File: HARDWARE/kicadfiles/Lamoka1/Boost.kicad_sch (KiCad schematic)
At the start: 50 parts, among them J1 Boostconverteroutput, J2 Boostconverterinput, J3 Groundconnection, Q1 CSD19531Q5A, Q2 CSD19531Q5A, Q3 CSD19531Q5A, Q4 CSD19531Q5A, Q5 AO3400A, U2 LM5122QMHE/NOPB, U3 LM5122QMHE/NOPB

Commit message: Reconfiguring the BOM, other misc tasks
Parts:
- C27: footprint Components:PCAP_10x10-ELECT_NCA -> Components:PCAP_8x10-ELECT_NCH
- C36: footprint Components:CAP_UCD2A_NCH -> Components:PCAP_8x10-ELECT_NCH
- J1, J2, J3, TP1, TP2, TP3, TP4, TP5, TP6, TP7, TP8: now left out of the parts list
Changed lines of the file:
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@@
 		(body_style 1)
 		(exclude_from_sim no)
-		(in_bom yes)
+		(in_bom no)
 		(on_board yes)
 		(in_pos_files yes)
@@
 		(body_style 1)
 		(exclude_from_sim no)
-		(in_bom yes)
+		(in_bom no)
 		(on_board yes)
 		(in_pos_files yes)
@@
 			)
 		)
-		(property "Datasheet" "C1206C224M1REC7210"
+		(property "Datasheet" "MPN: C1206C224M1REC7210"
 			(at 110.49 138.43 0)
 			(hide yes)
@@
 			)
 		)
-		(property "Datasheet" "https://search.murata.co.jp/Ceramy/image/img/A01X/G101/ENG/KRM55_25V-100V_E.pdf"
+		(property "Datasheet" "MPN: KRM55WR72A226MH01K"
 			(at 452.73 147.32 0)
 			(hide yes)
@@
 			)
 		)
-		(property "Datasheet" "RC0603FR-0736KL"
+		(property "Datasheet" "MPN: RC0603FR-0736KL"
 			(at 151.13 176.53 0)
 			(hide yes)
@@
 		(body_style 1)
 		(exclude_from_sim no)
-		(in_bom yes)
+		(in_bom no)
 		(on_board yes)
 		(in_pos_files yes)
@@
 			)
 		)
-		(property "Datasheet" "https://www.diodes.com/assets/Datasheets/SDM1U100S1F.pdf"
+		(property "Datasheet" "MPN: SDM1U100S1F-7"
 			(at -150.47 154.94 0)
 			(hide yes)
@@
 		(body_style 1)
 		(exclude_from_sim no)
-		(in_bom yes)
+		(in_bom no)
 		(on_board yes)
 		(in_pos_files yes)
@@
 			)
 		)
-		(property "Datasheet" "RN73R1JTTD4992F25"
+		(property "Datasheet" "MPN: RN73R1JTTD4992F25"
 			(at 35.56 30.48 0)
 			(hide yes)
@@
 			)
 		)
-		(property "Datasheet" "http://www.ti.com/lit/gpn/csd19531q5a"
+		(property "Datasheet" "MPN: CSD19531Q5A"
 			(at 113.03 40.64 0)
 			(hide yes)
@@
 			)
 		)
-		(property "Datasheet" "https://www.diodes.com/assets/Datasheets/SDM1U100S1F.pdf"
+		(property "Datasheet" "MPN: SDM1U100S1F-7"
 			(at -92.05 154.94 0)
 			(hide yes)
@@
 			)
 		)
-		(property "Datasheet" "RC0603FR-0756K2L"
+		(property "Datasheet" "MPN: RC0603FR-0756K2L"
 			(at 243.84 116.84 0)
 			(hide yes)
@@
 		(body_style 1)
 		(exclude_from_sim no)
-		(in_bom yes)
+		(in_bom no)
 		(on_board yes)
 		(in_pos_files yes)
@@
 			)
 		)
-		(property "Datasheet" "UUX2A470MNL1GS"
+		(property "Datasheet" "MPN: UUX2A470MNL1GS"
 			(at 27.94 64.77 0)
 			(hide yes)
@@
 			)
 		)
-		(property "Footprint" "Components:PCAP_10x10-ELECT_NCA"
+		(property "Footprint" "Components:PCAP_8x10-ELECT_NCH"
 			(at 36.83 63.5 0)
 			(hide yes)
@@
 			)
 		)
-		(property "Datasheet" "UCD2A220MNL1GS"
+		(property "Datasheet" "MPN: UCD2A220MNL1GS"
 			(at 36.83 63.5 0)
 			(hide yes)
@@
 		(body_style 1)
 		(exclude_from_sim no)
-		(in_bom yes)
+		(in_bom no)
 		(on_board yes)
 		(in_pos_files yes)
@@
 		(body_style 1)
 		(exclude_from_sim no)
-		(in_bom yes)
+		(in_bom no)
 		(on_board yes)
 		(in_pos_files yes)
@@
 			)
 		)
-		(property "Datasheet" "https://product.tdk.com/system/files/dam/doc/product/capacitor/ceramic/mlcc/catalog/mlcc_commercial_soft_cnc_en.pdf"
+		(property "Datasheet" "MPN: CNC5L1X7R1H106K160AE"
 			(at 91.44 334.62 0)
 			(hide yes)
@@
 		(body_style 1)
 		(exclude_from_sim no)
-		(in_bom yes)
+		(in_bom no)
 		(on_board yes)
 		(in_pos_files yes)
@@
 			)
 		)
-		(property "Datasheet" "http://www.ti.com/lit/gpn/csd19531q5a"
+		(property "Datasheet" "MPN: CSD19531Q5A"
 			(at 114.3 78.74 0)
 			(hide yes)
@@
 			)
 		)
-		(property "Datasheet" "http://www.ti.com/lit/gpn/csd19531q5a"
+		(property "Datasheet" "MPN: CSD19531Q5A"
 			(at 115.57 72.39 0)
 			(hide yes)
@@
 			)
 		)
-		(property "Datasheet" "RC0603FR-0710KL"
+		(property "Datasheet" "MPN: RC0603FR-0710KL"
 			(at 182.88 154.94 0)
 			(hide yes)
@@
 			)
 		)
-		(property "Datasheet" "https://www.te.com/commerce/DocumentDelivery/DDEController?Action=srchrtrv&DocNm=1773449-4&DocType=Data+Sheet&DocLang=English&PartCntxt=1-2176422-9&DocFormat=pdf"
+		(property "Datasheet" "MPN: TLRP3A30CR005FTE"
 			(at 59.69 63.5 0)
 			(hide yes)
@@
 			)
 		)
-		(property "Datasheet" "CL10B104KB8NNNC"
+		(property "Datasheet" "MPN: CL10B104KB8NNNC"
 			(at 83.82 35.56 0)
 			(hide yes)
@@
 			)
 		)
-		(property "Footprint" "Components:CAP_UCD2A_NCH"
+		(property "Footprint" "Components:PCAP_8x10-ELECT_NCH"
 			(at 266.7 148.59 0)
 			(hide yes)
@@
 			)
 		)
-		(property "Datasheet" "UCD2A101MNJ1MS"
+		(property "Datasheet" "MPN: UUX2A100MNL1GS"
 			(at 266.7 148.59 0)
 			(hide yes)
@@
 			)
 		)
-		(property "Datasheet" "UCD2A220MNL1GS"
+		(property "Datasheet" "MPN: UCD2A220MNL1GS"
 			(at 245.11 148.59 0)
 			(hide yes)
@@
 			)
 		)
-		(property "Datasheet" "https://content.kemet.com/datasheets/KEM_C1002_X7R_SMD.pdf"
+		(property "Datasheet" "MPN: C1206C474K1RACTU"
 			(at 196.85 135.89 0)
 			(hide yes)
@@
 			)
 		)
-		(property "Datasheet" "C1206C224M1REC7210"
+		(property "Datasheet" "MPN: C1206C224M1REC7210"
 			(at 50.8 138.43 0)
 			(hide yes)
@@
 			)
 		)
-		(property "Datasheet" "https://product.tdk.com/system/files/dam/doc/product/capacitor/ceramic/mlcc/catalog/mlcc_commercial_soft_cnc_en.pdf"
+		(property "Datasheet" "MPN: CNC5L1X7R1H106K160AE"
 			(at 33.02 334.62 0)
 			(hide yes)
@@
 			)
 		)
-		(property "Datasheet" "https://www.te.com/commerce/DocumentDelivery/DDEController?Action=srchrtrv&DocNm=1773449-4&DocType=Data+Sheet&DocLang=English&PartCntxt=1-2176422-9&DocFormat=pdf"
+		(property "Datasheet" "MPN: TLRP3A30CR005FTE"
 			(at 50.8 92.71 0)
 			(hide yes)
@@
 			)
 		)
-		(property "Datasheet" "https://www.we-online.com/catalog/datasheet/7443641000B.pdf?ki"
+		(property "Datasheet" "MPN: 7443641000B"
 			(at 135.89 45.72 0)
 			(hide yes)
@@
 			)
 		)
-		(property "Datasheet" ""
+		(property "Datasheet" "MPN: RN73R1JTTD1842B25"
 			(at 48.26 30.48 0)
 			(hide yes)
@@
 			)
 		)
-		(property "Datasheet" "https://www.we-online.com/catalog/datasheet/7443641000B.pdf?ki"
+		(property "Datasheet" "MPN: 7443641000B"
 			(at 132.08 74.93 0)
 			(hide yes)
@@
 			)
 		)
-		(property "Datasheet" "https://www.ti.com/lit/gpn/lm5122-q1"
+		(property "Datasheet" "MPN: LM5122QMHE/NOPB"
 			(at 181.61 20.32 0)
 			(hide yes)
@@
 		(body_style 1)
 		(exclude_from_sim no)
-		(in_bom yes)
+		(in_bom no)
 		(on_board yes)
 		(in_pos_files yes)
@@
 			)
 		)
-		(property "Datasheet" "http://www.ti.com/lit/gpn/csd19531q5a"
+		(property "Datasheet" "MPN: CSD19531Q5A"
 			(at 114.3 34.29 0)
 			(hide yes)
@@
 		(body_style 1)
 		(exclude_from_sim no)
-		(in_bom yes)
+		(in_bom no)
 		(on_board yes)
 		(in_pos_files yes)
@@
 			)
 		)
-		(property "Datasheet" "RC0603FR-0736KL"
+		(property "Datasheet" "MPN: RC0603FR-0736KL"
 			(at 162.56 124.46 0)
 			(hide yes)
@@
 			)
 		)
-		(property "Datasheet" "RC0603FR-07392KL"
+		(property "Datasheet" "MPN: RC0603FR-07392KL"
 			(at 208.28 154.94 0)
 			(hide yes)
@@
 			)
 		)
-		(property "Datasheet" "UUX2A470MNL1GS"
+		(property "Datasheet" "MPN: UUX2A470MNL1GS"
 			(at 19.05 63.5 0)
 			(hide yes)
@@
 			)
 		)
-		(property "Datasheet" "CC0603KRX7R9BB223"
+		(property "Datasheet" "MPN: CC0603KRX7R9BB223"
 			(at 257.81 116.84 0)
 			(hide yes)
@@
 			)
 		)
-		(property "Datasheet" "https://www.ti.com/lit/gpn/lm5122-q1"
+		(property "Datasheet" "MPN: LM5122QMHE/NOPB"
 			(at 181.61 55.88 0)
 			(hide yes)
@@
 			)
 		)
-		(property "Datasheet" "RC0805FR-0747KL"
+		(property "Datasheet" "MPN: RC0805FR-0747KL"
 			(at 74.93 180.34 0)
 			(hide yes)
@@
 			)
 		)
-		(property "Datasheet" "AO3400A"
+		(property "Datasheet" "MPN: AO3400A"
 			(at 29.21 175.26 0)
 			(hide yes)
@@
 			)
 		)
-		(property "Datasheet" "RC0603FR-0736KL"
+		(property "Datasheet" "MPN: RC0603FR-0736KL"
 			(at 132.08 163.83 0)
 			(hide yes)
@@
 		(body_style 1)
 		(exclude_from_sim no)
-		(in_bom yes)
+		(in_bom no)
 		(on_board yes)
 		(in_pos_files yes)

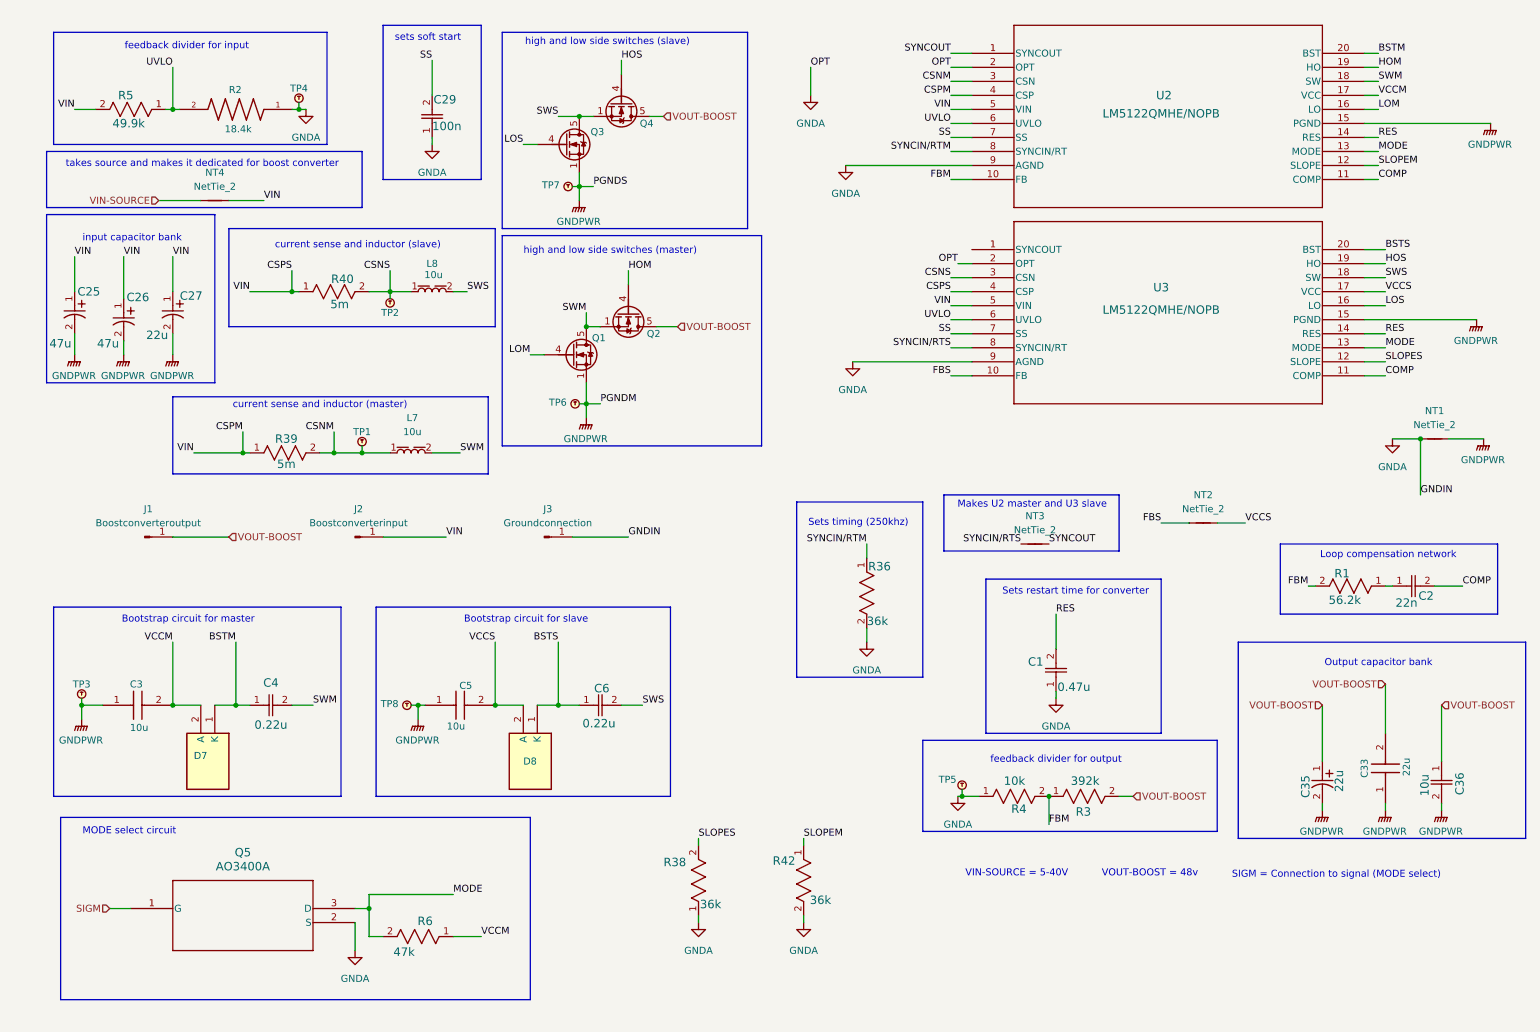
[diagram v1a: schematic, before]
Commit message: Take things out so boost converter can be standalone
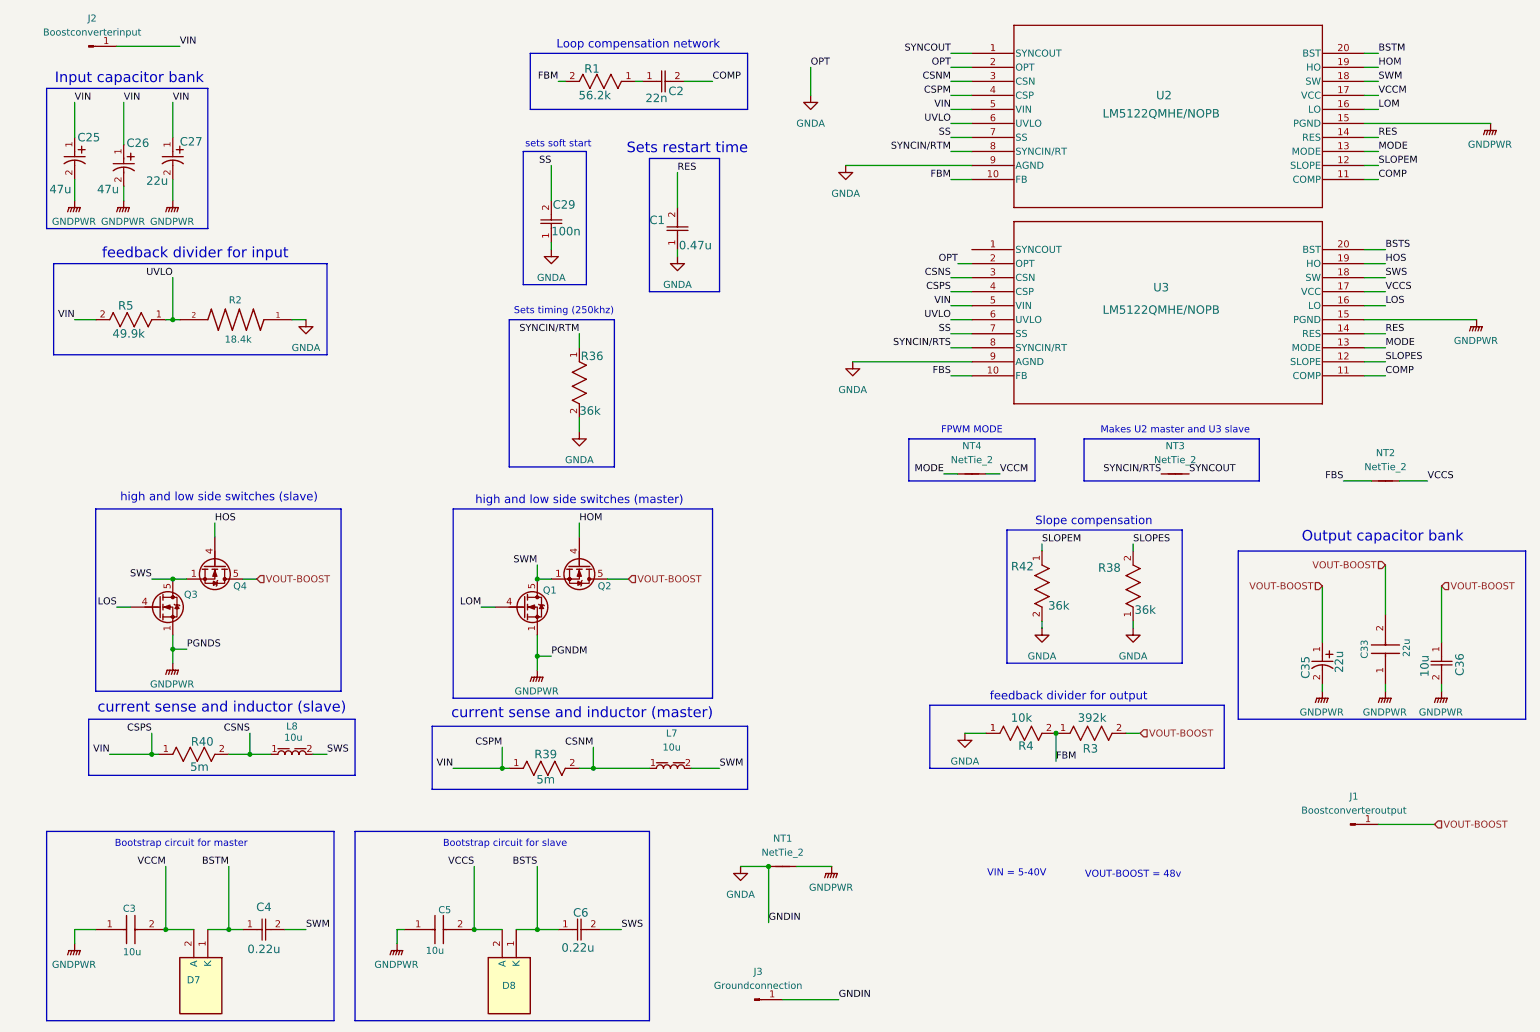
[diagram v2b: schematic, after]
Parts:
- removed Q5: AO3400A, Components:SOT-23-3L_AOS, symbol 2026-06-29_16-51-38:AO3400A
- removed R6: 47k, Components:RC0805N_YAG, symbol 2026-07-01_14-01-11:RC0805FR-0747KL
- removed TP1, TP3, TP4, TP5: Tomachie_TP_N, TestPoint:TestPoint_Pad_D2.0mm, symbol Pads:Tomachie_TP_N
- removed TP2: Tomachie_TP_S, TestPoint:TestPoint_Pad_D2.0mm, symbol Pads:Tomachie_TP_S
- removed TP6, TP7, TP8: Tomachie_TP_W, TestPoint:TestPoint_Pad_D2.0mm, symbol Pads:Tomachie_TP_W
- J1, J2, J3: footprint Connector_Wire:SolderWire-0.1sqmm_1x01_D0.4mm_OD1mm -> Connector_Wire:SolderWire-6sqmm_1x01_D3.5mm_OD7mm
- NT1, NT2, NT3, NT4: footprint NetTie:NetTie-2_SMD_Pad0.5mm -> NetTie:NetTie-2_SMD_Pad2.0mm
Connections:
- net VIN-SOURCE is gone; now on net MODE: NT4.1
- net CSPM: no longer NT4.2
- net VCCM: now also NT4.2
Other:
- note added: "FPWM MODE"
- note added: "Input capacitor bank"
- note added: "Sets restart time"
- note added: "Slope compensation"
- note added: "VIN = 5-40V"
- note removed: "MODE select circuit"
- note removed: "SIGM = Connection to signal (MODE select)"
- note removed: "Sets restart time for converter"
- note removed: "VIN-SOURCE = 5-40V"
- note removed: "input capacitor bank"
- note removed: "takes source and makes it dedicated for boost converter"
- moved on the sheet: C1, C2, C25, C26, C27, C29, C3, C33, C35, C36, C4, C5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

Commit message: Doing random things with the boost converter
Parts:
- NT2, NT4: footprint NetTie:NetTie-2_SMD_Pad2.0mm -> NetTie:NetTie-2_SMD_Pad0.5mm
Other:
- title: Boost-section -> Boost-section-prototype
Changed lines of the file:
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@@
 	(paper "A4")
 	(title_block
-		(title "Boost-section")
+		(title "Boost-section-prototype")
 		(date "2026")
-		(rev "1")
+		(rev "P1")
 		(company "Flamingo-n-Cactus")
 		(comment 1 "Designed in the US of A")
@@
 	)
 	(rectangle
-		(start 13.97 161.29)
+		(start 13.97 165.1)
 		(end 66.04 195.58)
 		(stroke
@@
 	)
 	(rectangle
-		(start 69.85 161.29)
+		(start 69.85 165.1)
 		(end 123.19 195.58)
 		(stroke
@@
 	(text "Bootstrap circuit for master"
 		(exclude_from_sim no)
-		(at 38.354 163.576 0)
+		(at 39.624 163.322 0)
 		(effects
 			(font
-				(size 1.27 1.27)
+				(size 1.524 1.524)
 			)
 		)
@@
 	(text "current sense and inductor (master)"
 		(exclude_from_sim no)
-		(at 110.998 139.954 0)
+		(at 111.252 140.716 0)
 		(effects
 			(font
@@
 	(text "high and low side switches (slave)"
 		(exclude_from_sim no)
-		(at 45.212 100.838 0)
+		(at 44.45 101.092 0)
 		(effects
 			(font
@@
 	(text "VOUT-BOOST = 48v"
 		(exclude_from_sim no)
-		(at 210.82 169.164 0)
+		(at 206.756 170.942 0)
 		(effects
 			(font
@@
 	(text "VIN = 5-40V"
 		(exclude_from_sim no)
-		(at 189.738 168.91 0)
+		(at 185.674 170.688 0)
 		(effects
 			(font
@@
 	(text "Bootstrap circuit for slave"
 		(exclude_from_sim no)
-		(at 97.028 163.576 0)
+		(at 96.774 163.576 0)
 		(effects
 			(font
-				(size 1.27 1.27)
+				(size 1.524 1.524)
 			)
 		)
@@
 		(in_pos_files yes)
 		(dnp no)
-		(fields_autoplaced yes)
 		(property "Reference" "NT4"
 			(at 181.61 91.44 0)
@@
 		)
 		(property "Value" "NetTie_2"
-			(at 181.61 93.98 0)
+			(at 181.61 93.218 0)
 			(show_name no)
 			(do_not_autoplace no)
@@
 			)
 		)
-		(property "Footprint" "NetTie:NetTie-2_SMD_Pad2.0mm"
+		(property "Footprint" "NetTie:NetTie-2_SMD_Pad0.5mm"
 			(at 181.61 96.52 0)
 			(hide yes)
@@
 		(in_pos_files yes)
 		(dnp no)
-		(fields_autoplaced yes)
 		(property "Reference" "NT2"
 			(at 256.54 92.71 0)
@@
 		)
 		(property "Value" "NetTie_2"
-			(at 256.54 95.25 0)
+			(at 256.54 94.488 0)
 			(show_name no)
 			(do_not_autoplace no)
@@
 			)
 		)
-		(property "Footprint" "NetTie:NetTie-2_SMD_Pad2.0mm"
+		(property "Footprint" "NetTie:NetTie-2_SMD_Pad0.5mm"
 			(at 256.54 97.79 0)
 			(hide yes)
@@
 		(in_pos_files yes)
 		(dnp no)
-		(fields_autoplaced yes)
 		(property "Reference" "NT3"
 			(at 218.44 91.44 0)
@@
 		)
 		(property "Value" "NetTie_2"
-			(at 218.44 93.98 0)
+			(at 218.44 93.218 0)
 			(show_name no)
 			(do_not_autoplace no)

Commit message: FIX make boost converter standalone
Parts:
- removed J2: Boostconverterinput, Connector_Wire:SolderWire-6sqmm_1x01_D3.5mm_OD7mm, symbol Connector:Conn_01x01_Pin
- removed J3: Groundconnection, Connector_Wire:SolderWire-6sqmm_1x01_D3.5mm_OD7mm, symbol Connector:Conn_01x01_Pin
- removed NT4: NetTie_2, NetTie:NetTie-2_SMD_Pad0.5mm, symbol Device:NetTie_2
- added NT5: NetTie_2, symbol Device:NetTie_2
- added Q5: BSS138, Components:SOT-23_3L_ONS, symbol 2026-07-06_18-33-39:BSS138
- added R7: 47k, Components:RC0603N_YAG, symbol 2026-07-06_18-22-10:RC0603FR-0747RL
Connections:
- net CSPM: now also NT5.2
- net GNDA: now also Q5.2 (S)
- net MODE: now also Q5.3 (D), R7.1
- net VCCM: now also R7.2
- new net SIGM: Q5.1 (G)
- new net VIN-SOURCE: NT5.1
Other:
- note added: "MODE select circuit"
- note added: "VIN-SOURCE = 5-40V"
- note removed: "FPWM MODE"
- note removed: "VIN = 5-40V"
- moved on the sheet: C1, C2, C29, L7, L8, NT1, Q1, Q2, Q3, Q4, R1, R3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
